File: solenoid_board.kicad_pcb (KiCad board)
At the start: 2 copper layers, 170 x 145 mm, 52 parts, among them J2 MCU_LEFT_LEGS, J3 MCU_RIGHT_LEGS

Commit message: Schematic Finished. Need to figure out geometry and route layout.
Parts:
- removed FET7: 2N7000, Package_TO_SOT_THT:TO-92_Inline
- removed R10k7: 10k, Resistor_THT:R_Axial_DIN0204_L3.6mm_D1.6mm_P5.08mm_Vertical
- removed R307: 300, Resistor_THT:R_Axial_DIN0204_L3.6mm_D1.6mm_P5.08mm_Vertical
- added C0.1uF0: 0.1 uF, Capacitor_THT:CP_Radial_D4.0mm_P2.00mm, F.Cu at (192.4, 47.8)
- added C0.1uF1: 0.1 uF, Capacitor_THT:CP_Radial_D4.0mm_P2.00mm, F.Cu at (198.0, 44.0)
- added Decoder0: Conn_02x08_Counter_Clockwise, digikey-footprints:DIP-16_W7.62mm, F.Cu at (170.6, 40.2)
- added Driver1: Conn_02x08_Counter_Clockwise, digikey-footprints:DIP-16_W7.62mm, F.Cu at (181.4, 40.2)
- added IN1: Conn_01x17, Connector_PinHeader_2.54mm:PinHeader_1x17_P2.54mm_Vertical, F.Cu at (166.7, 39.7)
- added JP0: Jumper_3_Open, Jumper:SolderJumper-3_P1.3mm_Open_RoundedPad1.0x1.5mm, F.Cu at (193.4, 39.2)
- added JP1: Jumper_3_Open, Jumper:SolderJumper-3_P1.3mm_Open_RoundedPad1.0x1.5mm, F.Cu at (199.0, 39.2)
- added JP10: Jumper_2_Open, Jumper:SolderJumper-2_P1.3mm_Open_RoundedPad1.0x1.5mm, F.Cu at (171.2, 65.1)
- added JP11: Jumper_2_Open, Jumper:SolderJumper-2_P1.3mm_Open_RoundedPad1.0x1.5mm, F.Cu at (175.5, 65.1)
- added JP12: Jumper_2_Open, Jumper:SolderJumper-2_P1.3mm_Open_RoundedPad1.0x1.5mm, F.Cu at (179.9, 65.1)
- added JP2: Jumper_3_Open, Jumper:SolderJumper-3_P1.3mm_Open_RoundedPad1.0x1.5mm, F.Cu at (204.7, 39.2)
- added JP3: Jumper_3_Open, Jumper:SolderJumper-3_P1.3mm_Open_RoundedPad1.0x1.5mm, F.Cu at (193.4, 43.0)
- added JP4: Jumper_2_Open, Jumper:SolderJumper-2_P1.3mm_Open_RoundedPad1.0x1.5mm, F.Cu at (171.2, 68.6)
- added JP5: Jumper_2_Open, Jumper:SolderJumper-2_P1.3mm_Open_RoundedPad1.0x1.5mm, F.Cu at (192.7, 52.4)
- added JP6: Jumper_2_Open, Jumper:SolderJumper-2_P1.3mm_Open_RoundedPad1.0x1.5mm, F.Cu at (171.2, 61.5)
- added JP7: Jumper_2_Open, Jumper:SolderJumper-2_P1.3mm_Open_RoundedPad1.0x1.5mm, F.Cu at (175.5, 61.5)
- added JP8: Jumper_2_Open, Jumper:SolderJumper-2_P1.3mm_Open_RoundedPad1.0x1.5mm, F.Cu at (179.9, 61.5)
- added JP9: Jumper_2_Open, Jumper:SolderJumper-2_P1.3mm_Open_RoundedPad1.0x1.5mm, F.Cu at (184.2, 61.5)
- added OUT1: Conn_01x17, Connector_PinHeader_2.54mm:PinHeader_1x17_P2.54mm_Vertical, F.Cu at (162.0, 39.7)
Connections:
- J2 pad 10: /A5 -> (no net)
- J2 pad 11: /SCK -> (no net)
- J2 pad 12: /MOSI -> (no net)
- J3 pad 10: (no net) -> /D5
- J3 pad 11: (no net) -> /SCL
- J3 pad 12: (no net) -> /SDA
- J3 pad 8: (no net) -> /D9
- J3 pad 9: (no net) -> /D6
- R10k0 pad 1: /A0 -> /_a
- R10k1 pad 1: /A1 -> /_b
- R10k10 pad 1: /D11 -> /K2
- R10k11 pad 1: /D10 -> /K3
- R10k2 pad 1: /A2 -> /_c
- R10k3 pad 1: /A3 -> /_d
- R10k4 pad 1: /A5 -> /_e
- R10k5 pad 1: /SCK -> /_f
- R10k6 pad 1: /MOSI -> /_g
- R10k8 pad 1: /D13 -> /K0
- R10k9 pad 1: /D12 -> /K1

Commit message: Serious Geometry design occurred.
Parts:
- added REF**: MountingHole_2.7mm_M2.5, MountingHole:MountingHole_2.7mm_M2.5, F.Cu at (140.0, 57.0)
- added REF**: MountingHole_2.7mm_M2.5, MountingHole:MountingHole_2.7mm_M2.5, F.Cu at (140.0, 147.0)
- added REF**: MountingHole_2.7mm_M2.5, MountingHole:MountingHole_2.7mm_M2.5, F.Cu at (101.9, 147.0)
- added REF**: MountingHole_2.7mm_M2.5, MountingHole:MountingHole_2.7mm_M2.5, F.Cu at (101.9, 57.0)
- added REF**: MountingHole_2.7mm_M2.5, MountingHole:MountingHole_2.7mm_M2.5, F.Cu at (50.0, 57.0)
- added REF**: MountingHole_2.7mm_M2.5, MountingHole:MountingHole_2.7mm_M2.5, F.Cu at (50.0, 147.0)
- 7Seg_2, 7Seg_3, 7Seg_4: moved to B.Cu
- R10, R11: footprint Resistor_THT:R_Axial_DIN0309_L9.0mm_D3.2mm_P20.32mm_Horizontal -> Resistor_THT:R_Axial_DIN0204_L3.6mm_D1.6mm_P5.08mm_Vertical
- moved IN1 153.6 mm to (55.7, 146.0), turned to 90 degrees
- moved OUT1 153.2 mm to (55.7, 150.0), turned to 90 degrees
- moved R10k10 104.8 mm to (133.1, 33.0)
- moved R10k8 104.8 mm to (141.3, 33.0)
- moved R300 104.8 mm to (125.0, 33.0)
- moved R304 104.8 mm to (149.4, 33.0)
- moved R10k4 92.6 mm to (150.4, 44.1)
- moved R10k9 92.6 mm to (142.2, 44.1)
- moved R301 92.6 mm to (134.1, 44.1)
- moved R10k11 87.7 mm to (113.0, 43.2)
- moved C0.1nF0 78.5 mm to (125.0, 101.4)
- moved RS-485 78.5 mm to (118.2, 98.6)
- moved 7Seg_1 71.4 mm to (85.5, 110.8), turned to 0 degrees
- moved CP0 71.1 mm to (137.4, 70.4)
- moved J3 71.1 mm to (133.8, 65.3)
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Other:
- board size 170 x 145 mm -> 100 x 100 mm

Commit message: Worked Geometry to 40% mark.
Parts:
- removed C0.1uF0: 0.1 uF, Capacitor_THT:CP_Radial_D4.0mm_P2.00mm
- Driver1: moved to B.Cu
- moved C0.1uF1 201.3 mm to (97.0, 138.0)
- moved Decoder0 179.1 mm to (93.5, 130.2), turned to 270 degrees
- moved FET0 161.1 mm to (70.5, 30.5)
- moved R10k0 152.3 mm to (66.5, 25.0)
- moved FET1 148.9 mm to (83.5, 30.5)
- moved Driver1 139.6 mm to (119.2, 73.0)
- moved R10k1 129.0 mm to (79.8, 24.8)
- moved R10k8 114.1 mm to (201.0, 130.2)
- moved R10k10 112.9 mm to (172.6, 138.8)
- moved R10k4 112.9 mm to (189.9, 149.9)
- moved R10k9 112.9 mm to (181.7, 149.9)
- moved R304 112.9 mm to (188.9, 138.8)
- moved COMMS0 111.0 mm to (107.8, 55.2)
- moved COMMS1 98.2 mm to (107.8, 62.2)
- moved FET6 88.2 mm to (158.8, 26.8)
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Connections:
- IN1 pad 10: /Y6 -> /Y5
- IN1 pad 11: /Y7 -> /Y4
- IN1 pad 8: /Y4 -> /Y7
- IN1 pad 9: /Y5 -> /Y6
- OUT1 pad 10: /Y6 -> /Y5
- OUT1 pad 11: /Y7 -> /Y4
- OUT1 pad 8: /Y4 -> /Y7
- OUT1 pad 9: /Y5 -> /Y6
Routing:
- net /B: track 0.00 -> 37.9 mm
- net /A: track 0.00 -> 34.7 mm
- net +3V3: track 0.00 -> 33.9 mm
- net +5V: track 0.00 -> 33.5 mm
- net /_d: track 0.00 -> 31.8 mm
- net /_e: track 0.00 -> 30.5 mm
- net /D10: track 0.00 -> 27.0 mm
- net /D9: track 0.00 -> 23.7 mm
- net /A3: track 0.00 -> 23.6 mm
- net /D6: track 0.00 -> 22.4 mm
- net /Y3: track 0.00 -> 22.4 mm
- net /Y7: track 0.00 -> 21.4 mm
- net /TX1: track 0.00 -> 20.7 mm, vias 0 -> 1
- net /D5: track 0.00 -> 19.3 mm
- net /_c: track 0.00 -> 17.5 mm
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
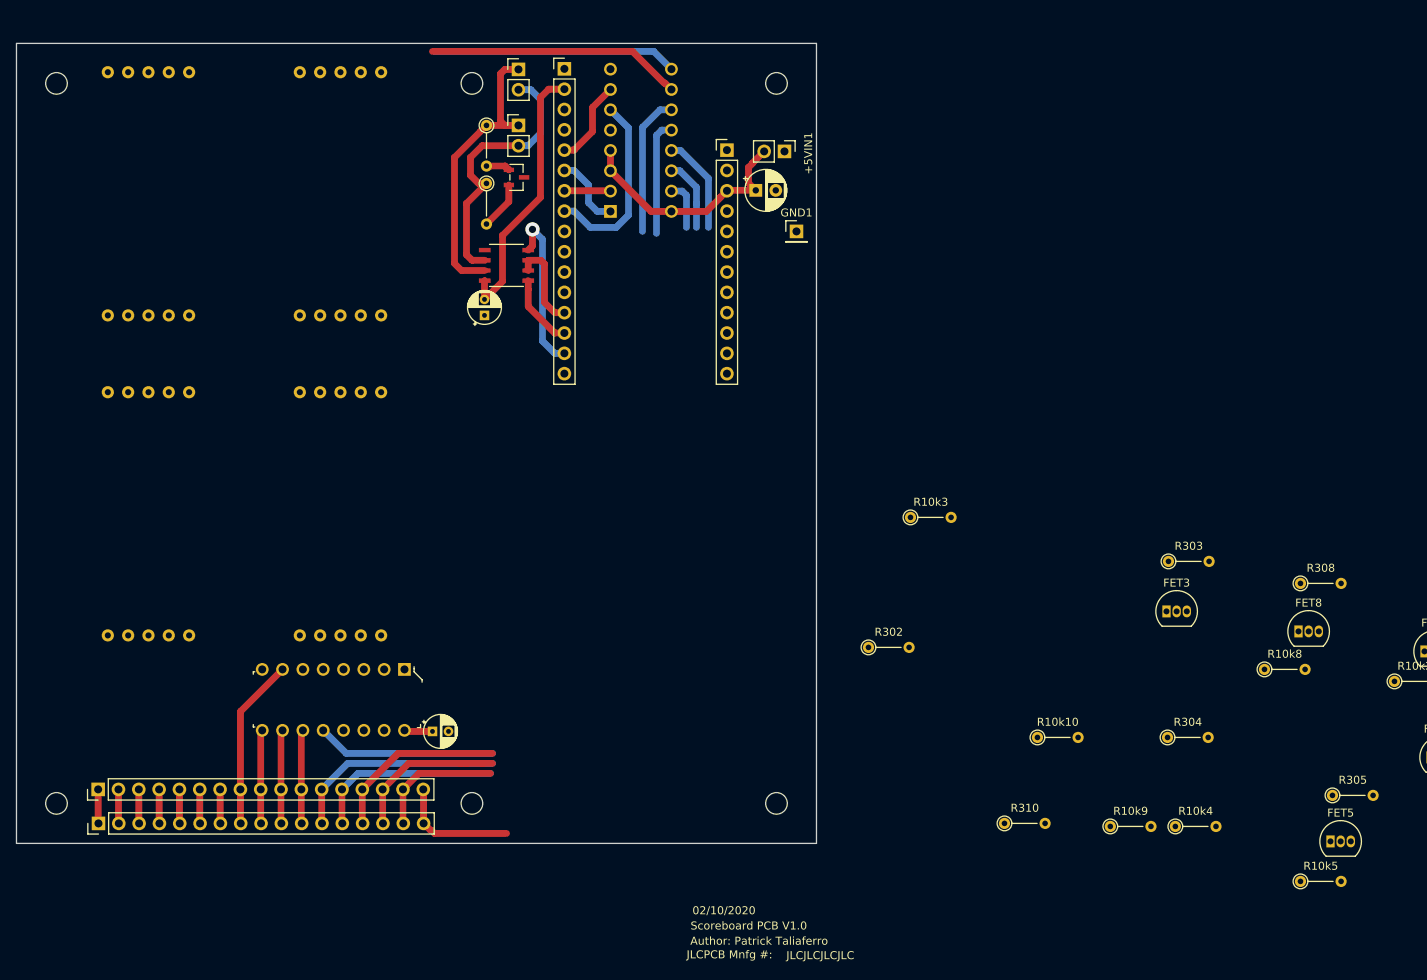
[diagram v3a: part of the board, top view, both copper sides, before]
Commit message: Changed Geometry significantly.
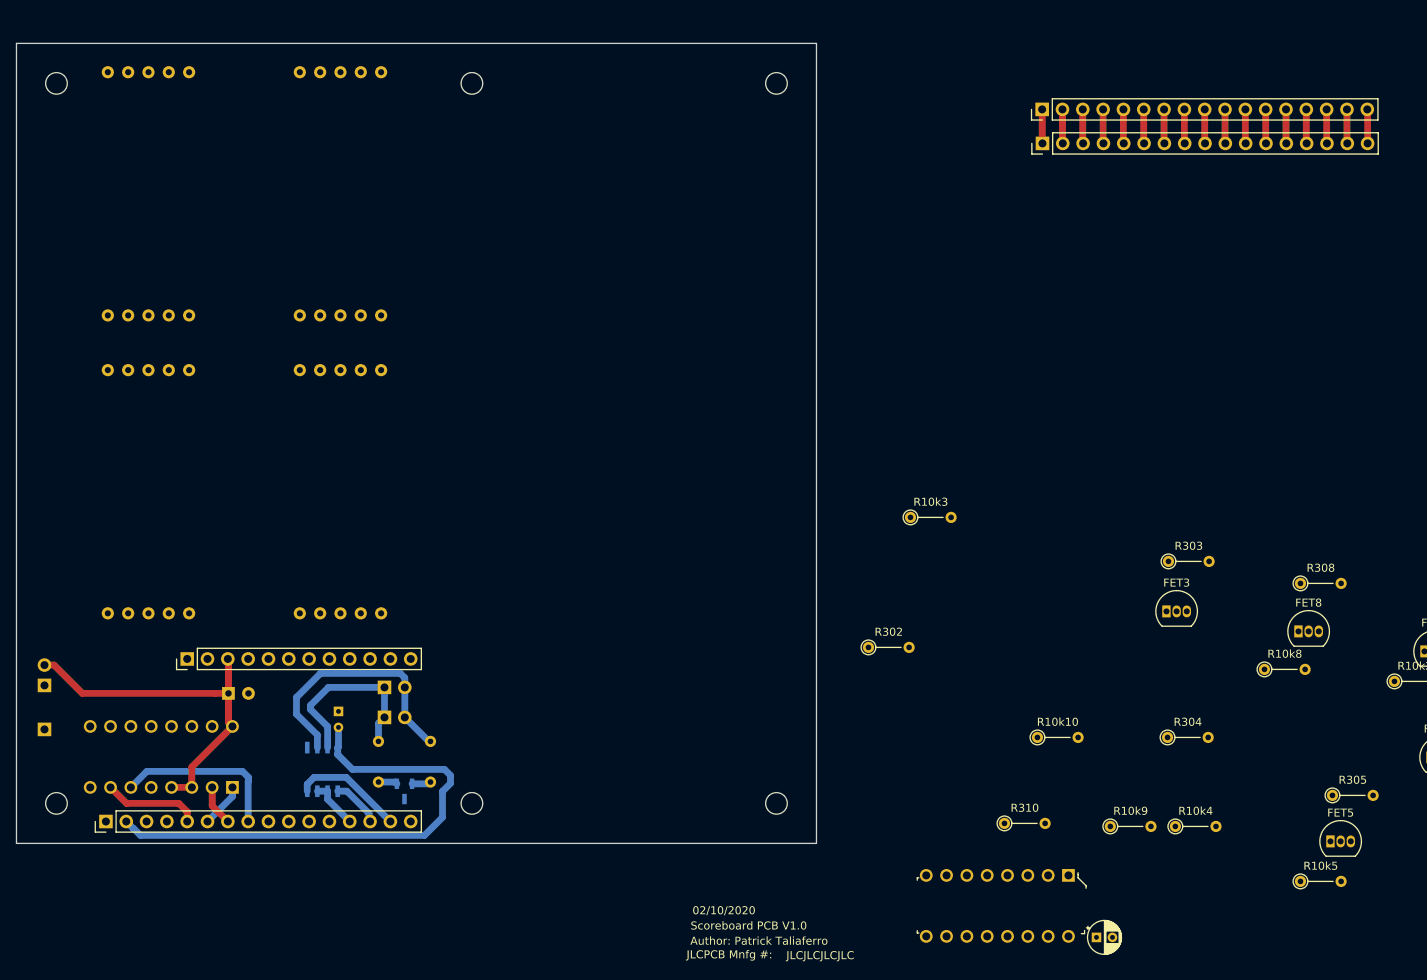
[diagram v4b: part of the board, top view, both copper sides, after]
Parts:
- +5VIN1, C0.1nF0, COMMS0, COMMS1, CP0, GND1, Prt_IC1, R10, R11, RS-485: moved to B.Cu
- moved IN1 145.4 mm to (173.2, 60.2)
- moved OUT1 145.4 mm to (173.2, 64.5)
- moved +5VIN1 114.1 mm to (48.5, 132.2), turned to 0 degrees
- moved GND1 112.7 mm to (48.5, 137.8)
- moved J2 110.2 mm to (56.2, 149.3), turned to 90 degrees
- moved J3 92.7 mm to (66.3, 128.9), turned to 90 degrees
- moved CP0 91.1 mm to (71.5, 133.2)
- moved C0.1uF1 86.9 mm to (180.0, 163.8)
- moved Decoder0 86.9 mm to (176.5, 156.0)
- moved Driver1 86.1 mm to (72.0, 145.0), turned to 90 degrees
- moved COMMS0 82.7 mm to (91.0, 136.2), turned to 270 degrees
- moved R11 78.2 mm to (90.2, 139.2)
- moved Prt_IC1 78.0 mm to (93.5, 145.5), turned to 0 degrees
- moved COMMS1 72.2 mm to (91.0, 132.5), turned to 270 degrees
- moved R10 70.1 mm to (96.8, 139.2)
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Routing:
- net /_d: track 31.8 -> 0.00 mm
- net +3V3: track 33.9 -> 65.5 mm
- net /_e: track 30.5 -> 0.00 mm
- net /D10: track 27.0 -> 4.27 mm
- net /Y3: track 22.4 -> 0.00 mm
- net /D9: track 23.7 -> 4.27 mm
- net /D6: track 22.4 -> 4.27 mm
- net /_c: track 17.5 -> 0.00 mm
- net /Y7: track 21.4 -> 4.27 mm
- net /D5: track 19.3 -> 4.27 mm
- net /B: track 37.9 -> 23.4 mm
- net /_b: track 14.4 -> 0.00 mm
- net /_a: track 12.2 -> 0.00 mm
- net +5V: track 33.5 -> 45.4 mm
- net /SCL: track 16.0 -> 4.27 mm
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
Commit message: Revised Schematic based on Dr. Fuch's suggested edits. Need to finalize Geometry and update BOM.
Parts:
- removed FET0, FET10, FET11, FET9: 2N7000, Package_TO_SOT_THT:TO-92_Inline
- removed IN1, OUT1: Conn_01x17, Connector_PinHeader_2.54mm:PinHeader_1x17_P2.54mm_Vertical
- removed JP0, JP1, JP2, JP3: Jumper_3_Open, Jumper:SolderJumper-3_P1.3mm_Open_RoundedPad1.0x1.5mm
- removed JP10, JP11, JP12, JP4, JP5, JP6, JP7, JP8, JP9: Jumper_2_Open, Jumper:SolderJumper-2_P1.3mm_Open_RoundedPad1.0x1.5mm
- removed R10k0, R10k10, R10k11, R10k9: 10k, Resistor_THT:R_Axial_DIN0204_L3.6mm_D1.6mm_P5.08mm_Vertical
- removed R300, R301, R302, R303, R304, R305, R306, R308, R309, R310, R311: 300, Resistor_THT:R_Axial_DIN0204_L3.6mm_D1.6mm_P5.08mm_Vertical
- removed REF** (x6): MountingHole_2.7mm_M2.5, MountingHole:MountingHole_2.7mm_M2.5
- added 7Seg_5: Conn_02x05_Top_Bottom, Kingbright_10-DinDisplay:SC10-21SRWA, B.Cu at (145.0, 90.0)
- added 7Seg_6: Conn_02x05_Top_Bottom, Kingbright_10-DinDisplay:SC10-21SRWA, B.Cu at (125.0, 90.0)
- added 7Seg_7: Conn_02x05_Top_Bottom, Kingbright_10-DinDisplay:SC10-21SRWA, B.Cu at (105.0, 90.0)
- added 7Seg_8: Conn_02x05_Top_Bottom, Kingbright_10-DinDisplay:SC10-21SRWA, B.Cu at (85.0, 90.0)
- added C0.1uF0: 0.1 uF, Capacitor_THT:CP_Radial_D4.0mm_P2.00mm, F.Cu at (116.0, 30.8)
- added FET7: 2N7000, Package_TO_SOT_THT:TO-92_Inline, F.Cu at (258.2, 44.8)
- added R101: 100, Resistor_THT:R_Axial_DIN0204_L3.6mm_D1.6mm_P5.08mm_Vertical, F.Cu at (203.2, 50.0)
- added R102: 100, Resistor_THT:R_Axial_DIN0204_L3.6mm_D1.6mm_P5.08mm_Vertical, F.Cu at (213.0, 50.5)
- added R103: 100, Resistor_THT:R_Axial_DIN0204_L3.6mm_D1.6mm_P5.08mm_Vertical, F.Cu at (220.8, 51.0)
- added R104: 100, Resistor_THT:R_Axial_DIN0204_L3.6mm_D1.6mm_P5.08mm_Vertical, F.Cu at (229.2, 52.0)
- added R105: 100, Resistor_THT:R_Axial_DIN0204_L3.6mm_D1.6mm_P5.08mm_Vertical, F.Cu at (238.0, 52.0)
- added R106: 100, Resistor_THT:R_Axial_DIN0204_L3.6mm_D1.6mm_P5.08mm_Vertical, F.Cu at (246.7, 52.2)
- added R107: 100, Resistor_THT:R_Axial_DIN0204_L3.6mm_D1.6mm_P5.08mm_Vertical, F.Cu at (257.0, 52.5)
- added R108: 100, Resistor_THT:R_Axial_DIN0204_L3.6mm_D1.6mm_P5.08mm_Vertical, F.Cu at (266.5, 53.2)
- added R10k7: 10k, Resistor_THT:R_Axial_DIN0204_L3.6mm_D1.6mm_P5.08mm_Vertical, F.Cu at (257.5, 58.8)
- +5VIN1, C0.1nF0, COMMS0, COMMS1, CP0, Driver1, GND1, Prt_IC1, R10, R11, RS-485: moved to F.Cu
- moved Decoder0 144.1 mm to (104.8, 31.0), turned to 0 degrees
- moved C0.1uF1 138.0 mm to (141.5, 31.2)
- moved R10k1 130.1 mm to (205.2, 59.0)
- moved Driver1 127.6 mm to (129.8, 31.2), turned to 0 degrees
- moved FET1 123.5 mm to (206.2, 43.8)
- moved J2 120.9 mm to (49.8, 28.5), turned to 0 degrees
- moved 7Seg_2 118.6 mm to (165.0, 50.0), turned to 180 degrees
- moved 7Seg_1 115.2 mm to (185.0, 50.0), turned to 180 degrees
- moved +5VIN1 112.5 mm to (80.8, 24.5), turned to 270 degrees
- moved FET5 112.4 mm to (240.2, 43.8)
- moved GND1 111.0 mm to (89.2, 34.5)
- moved 7Seg_4 105.3 mm to (165.0, 90.0), turned to 180 degrees
- moved FET8 103.6 mm to (268.2, 43.2)
- moved R10k5 103.3 mm to (238.2, 58.8)
- moved 7Seg_3 101.3 mm to (185.0, 90.0), turned to 180 degrees
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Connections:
- 7Seg_3 pad 8: (no net) -> /Third_Display
- Decoder0 pad 1: /I0 -> /D13
- Decoder0 pad 2: /I1 -> /D12
- Decoder0 pad 3: /I2 -> /D11
- Driver1 pad 1: /A1 -> /D9
- Driver1 pad 10: /_d -> /d
- Driver1 pad 11: /_c -> /c
- Driver1 pad 12: /_b -> /b
- Driver1 pad 13: /_a -> /a
- Driver1 pad 14: /_g -> /g
- Driver1 pad 15: /_f -> /f
- Driver1 pad 2: /A2 -> /D6
- Driver1 pad 6: /A3 -> /D5
- Driver1 pad 7: /A0 -> /D10
- Driver1 pad 9: /_e -> /e
- FET1 pad 1: Net-(FET1-Pad1) -> /First_Display
- FET1 pad 3: /b -> GND
- FET2 pad 1: Net-(FET2-Pad1) -> /Second_Display
- FET2 pad 3: /c -> GND
- FET3 pad 1: Net-(FET3-Pad1) -> /Third_Display
- FET3 pad 3: /d -> GND
- FET4 pad 1: Net-(FET4-Pad1) -> /Fourth_Display
- FET4 pad 3: /e -> GND
- FET5 pad 1: Net-(FET5-Pad1) -> /Fifth_Display
- FET5 pad 3: /f -> GND
- FET6 pad 1: Net-(FET6-Pad1) -> /Sixth_Display
- FET6 pad 3: /g -> GND
- FET8 pad 1: Net-(FET8-Pad1) -> /Eighth_Display
- J2 pad 1: (no net) -> /RST
- J2 pad 10: (no net) -> /A5
- J2 pad 11: (no net) -> /SCK
- J2 pad 12: (no net) -> /MOSI
- J2 pad 3: (no net) -> /ARf
- J2 pad 9: (no net) -> /A4
- J3 pad 1: (no net) -> /BAT
- J3 pad 2: (no net) -> /En
- R10k1 pad 1: /_b -> /Y0
- R10k1 pad 2: Net-(FET1-Pad2) -> GND
- R10k2 pad 1: /_c -> /Y1
- R10k2 pad 2: Net-(FET2-Pad2) -> GND
- R10k3 pad 1: /_d -> /Y2
- R10k3 pad 2: Net-(FET3-Pad2) -> GND
- R10k4 pad 1: /_e -> /Y3
- R10k4 pad 2: Net-(FET4-Pad2) -> GND
- R10k5 pad 1: /_f -> /Y4
- R10k5 pad 2: Net-(FET5-Pad2) -> GND
- R10k6 pad 1: /_g -> /Y5
- R10k6 pad 2: Net-(FET6-Pad2) -> GND
- R10k8 pad 1: /K0 -> /Y7
- R10k8 pad 2: Net-(FET8-Pad2) -> GND
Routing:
- net +3V3: track 65.5 -> 0.00 mm
- net +5V: track 45.4 -> 0.00 mm
- net /A: track 31.8 -> 0.00 mm
- net /B: track 23.4 -> 0.00 mm
- net /A3: track 21.4 -> 0.00 mm
- net /TX1: track 13.9 -> 0.00 mm
- net /A0: track 12.1 -> 0.00 mm
- net /MISO: track 6.21 -> 0.00 mm
- net /RX0: track 6.13 -> 0.00 mm
- net /A1: track 5.55 -> 0.00 mm
- net /A2: track 5.08 -> 0.00 mm
- net /g: track 4.27 -> 0.00 mm
- net /c: track 4.27 -> 0.00 mm
- net /Y5: track 4.27 -> 0.00 mm
- net /D6: track 4.27 -> 0.00 mm
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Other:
- board outline removed
- board text removed: "02/10/2020"
- board text removed: "Author: Patrick Taliaferro"
- board text removed: "JLCJLCJLCJLC"
- board text removed: "JLCPCB Mnfg #:"
- board text removed: "Scoreboard PCB V1.0"
